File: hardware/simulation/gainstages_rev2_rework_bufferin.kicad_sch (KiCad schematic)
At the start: 25 parts, among them U1 ${SIM.PARAMS}, U2 ${SIM.PARAMS}, U3 ${SIM.PARAMS}

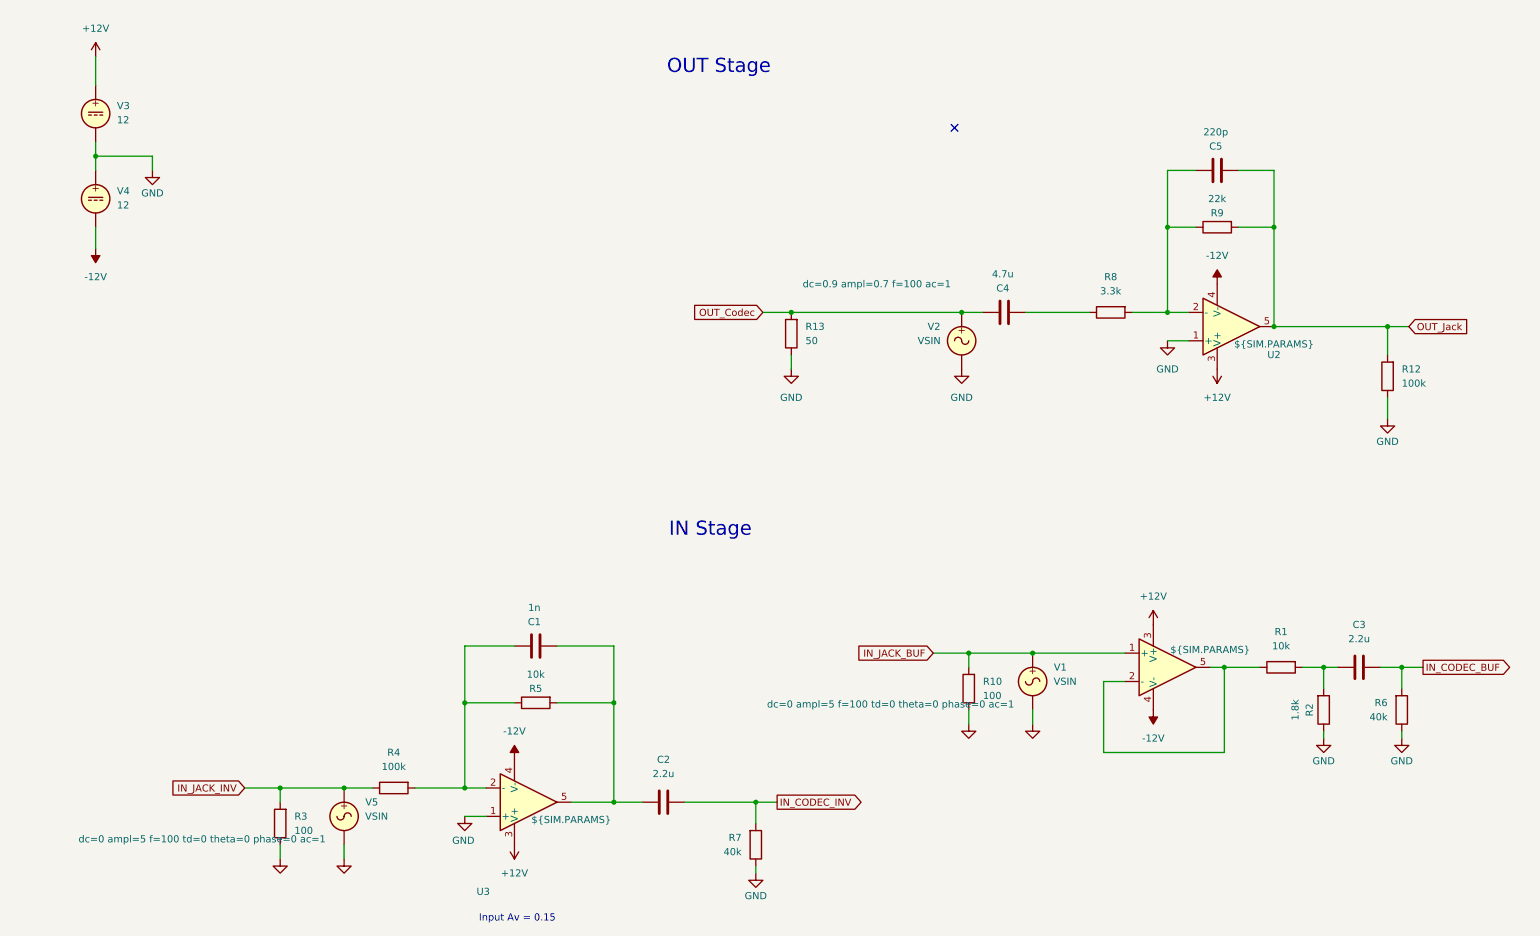
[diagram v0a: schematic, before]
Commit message: hwardware: update analog stages simulation
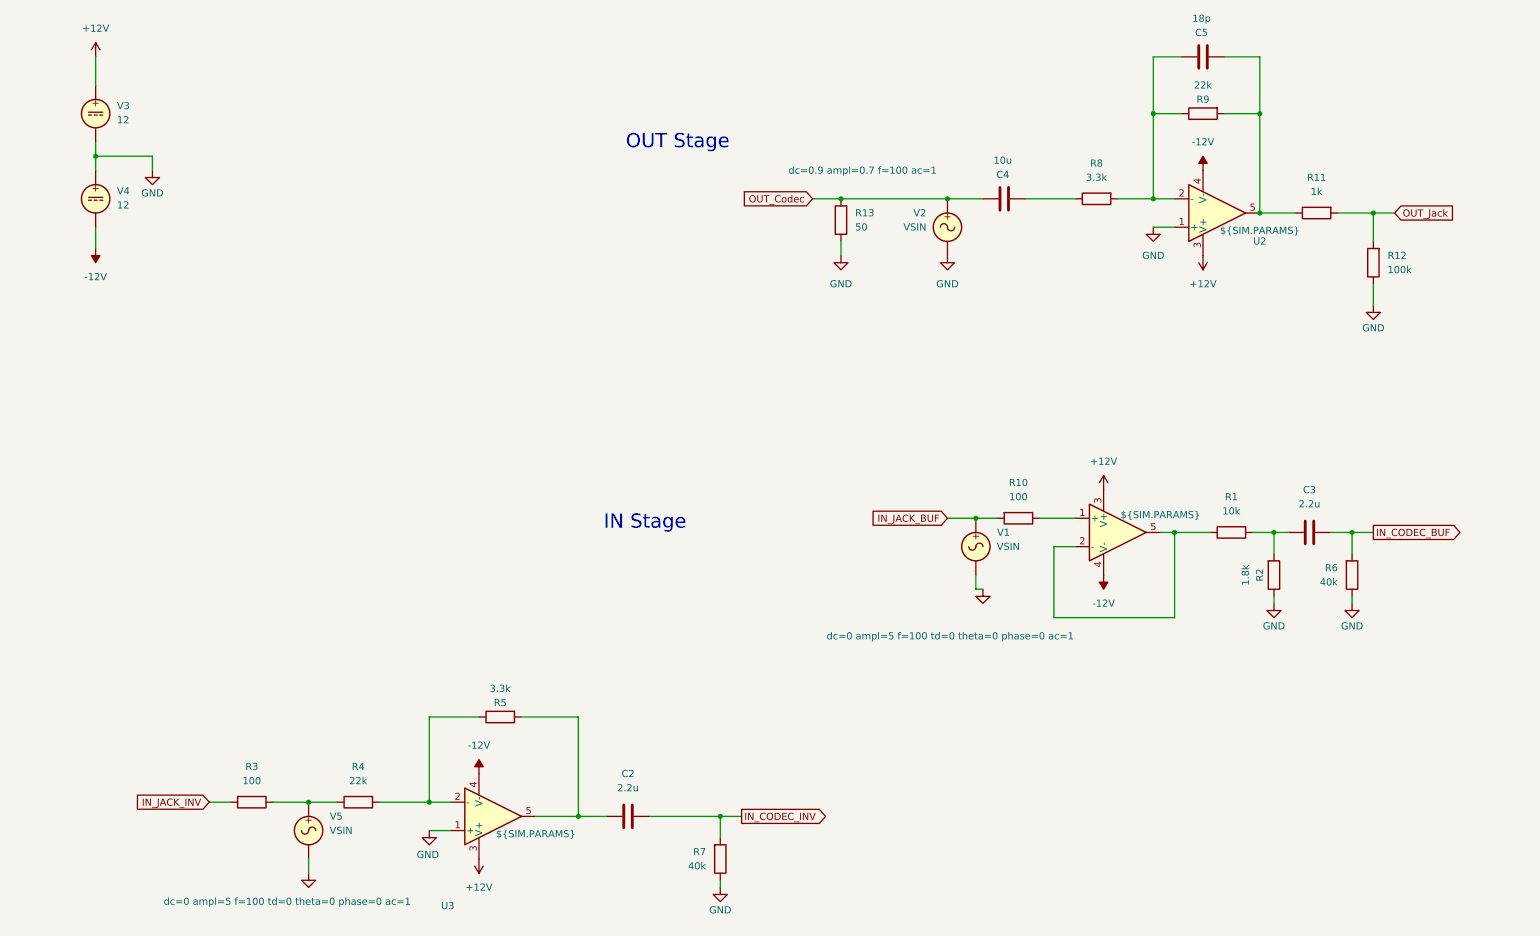
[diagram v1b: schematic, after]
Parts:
- removed C1: 1n, symbol Device:C
- added R11: 1k, symbol Device:R
- C4: value 4.7u -> 10u
- C5: value 220p -> 18p
- R4: value 100k -> 22k
- R5: value 10k -> 3.3k
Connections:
- net GND: no longer R10.1, R3.1
- net IN_JACK_BUF: no longer U1.1 (+)
- net IN_JACK_INV: no longer R4.1, V5.1
- net OUT_Jack: now also R11.2; no longer C5.1, R9.2, U2.5
- new net: R3.1, R4.1, V5.1
- new net: R10.1, U1.1 (+)
- new net: C5.1, R11.1, R9.2, U2.5
- no-connect marks 1 -> 0
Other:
- note removed: "Input Av = 0.15"
- moved on the sheet: C2, C3, C4, C5, R1, R12, R13, R2, R3, R4, R5, R6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

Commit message: hardware: update analog sim and routing (wip)
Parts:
- removed C5: 18p, symbol Device:C
- added C1: 18p, symbol Device:C
- added D1, D2: D_Schottky, symbol Device:D_Schottky
- added V10: 1.8, symbol Simulation_SPICE:VDC
- added V6: 3.3, symbol Simulation_SPICE:VDC
- added V7: 0.9, symbol Simulation_SPICE:VDC
- added V8, V9: VPULSE, symbol Simulation_SPICE:VPULSE
- R1: value 10k -> 12k
- R8: value 3.3k -> 5.6k
- R9: value 22k -> 39k
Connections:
- net GND: now also D2.1 (K), V10.2, V6.2, V7.2, V8.2, V9.2; no longer R13.1, R6.1
- net IN_CODEC_BUF: now also D1.1 (K), D2.2 (A)
- net IN_JACK_BUF: now also V9.1
- net OUT_Codec: now also V8.1; no longer C4.2
- net at R8.2, R9.1, U2.2 (-): now also C1.2
- net at R11.1, R9.2, U2.5: now also C1.1
- new net: R6.1, V7.1
- new net: C4.2, R13.1
- new net +1V8: D1.2 (A), V10.1
- new net +3V3: V6.1
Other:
- note added: "ADC absolute input limits: Input pins must remain within -0.3 V to (A_VDD + 0.3 V). Since A_VDD = 1.8 V (generated by the TLV320AIC internal LDO), the maximum allowed input voltage is 2.1 V. Therefore a voltage divider of 1.8k/12k=0.15 is used to attenuate the signal. The attenuation yields a peak voltage of 2.11V at -+10V input signal, which is just within the limits of the ADC. Such high signal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"
- note added: "CM (Common Mode) voltage of 0.9V"
- note added: "DAC Output Impedance"
- note added: "Downstream Input Impedance"
- note added: "Input AC Coupling filter Cutoff frequency f_c = 1/2*pi*R1*C3 = 1.809Hz"
- note added: "Input AC Coupling filter Cutoff frequency f_c = 1/2*pi*R13*C4 = 2.842Hz"
- note added: "Stabilization Filter prohibits Opamp Oscillation by input stray capacitances (not simulated) Cutoff frequency f = 1/2*pi*39E3*18E-12 = 226.716kHz"
- moved on the sheet: C2, C3, C4, R1, R10, R11, R12, R13, R2, R3, R4, R5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

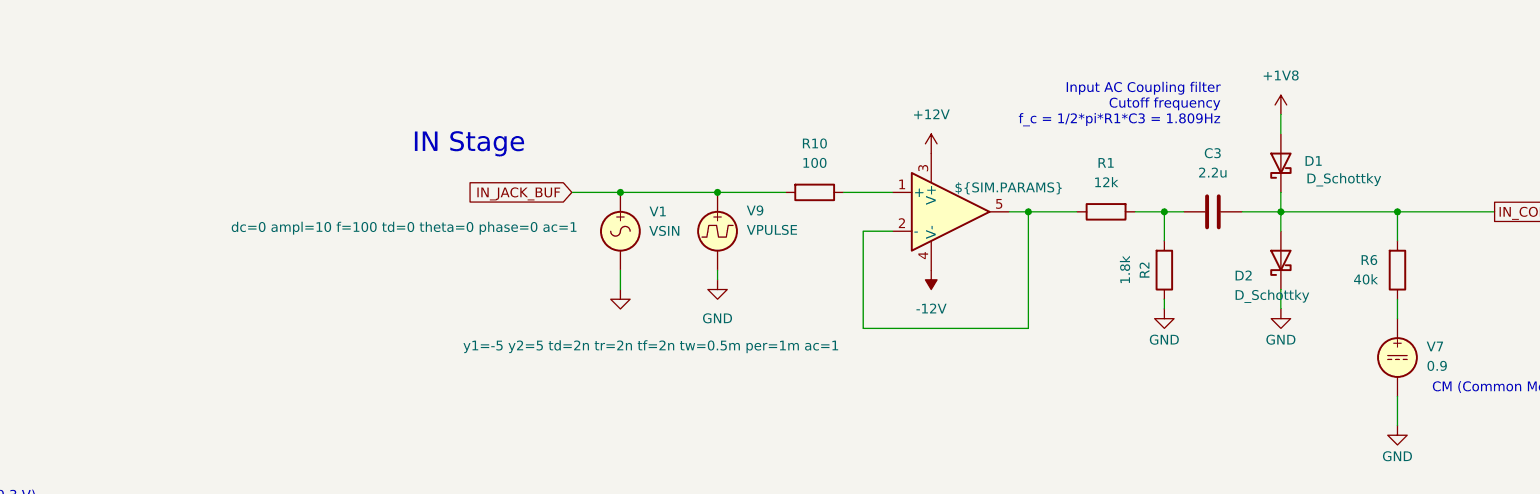
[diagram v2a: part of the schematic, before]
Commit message: sim: update simulation schematic and libraries
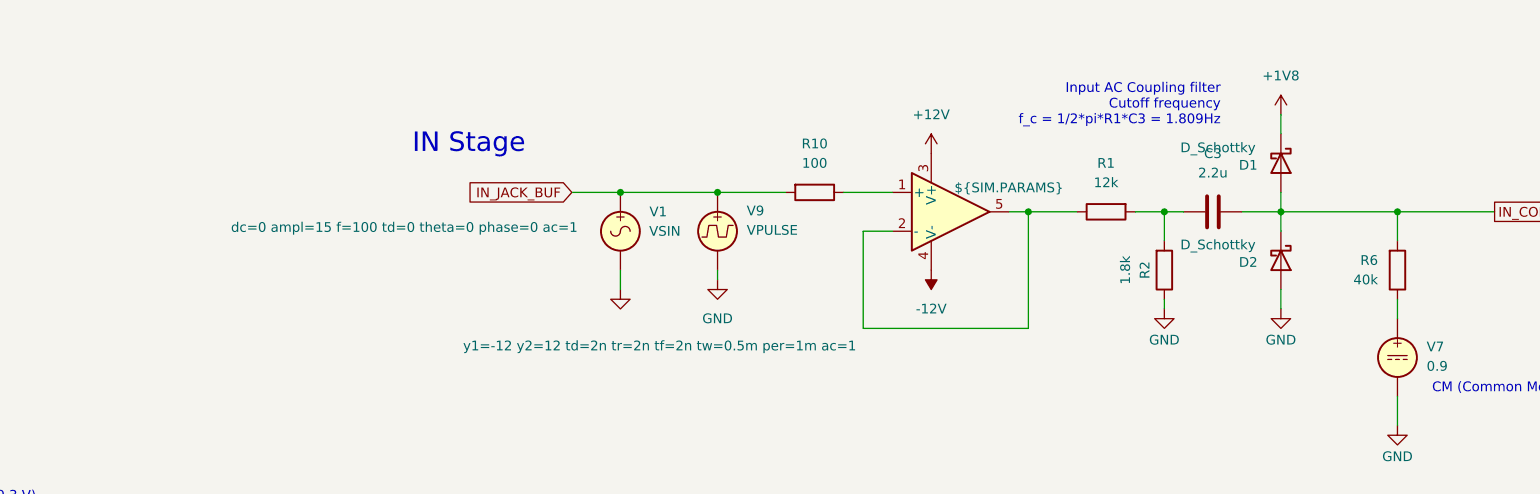
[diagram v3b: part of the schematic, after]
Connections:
- net +1V8: now also D1.1 (K); no longer D1.2 (A)
- net GND: now also D2.2 (A); no longer D2.1 (K)
- net IN_CODEC_BUF: now also D1.2 (A), D2.1 (K); no longer D1.1 (K), D2.2 (A)
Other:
- moved on the sheet: D1
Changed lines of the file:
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@@
 			)
 		)
-		(property "Sim.Pins" "1=1 2=2 3=3 4=4 5=5"
+		(property "Sim.Pins" "1=in+ 2=in- 3=vcc 4=vee 5=out"
 			(at 203.2 69.85 0)
 			(effects
@@
 			)
 		)
-		(property "Sim.Library" "/home/jonas/Downloads/NE5532.lib"
+		(property "Sim.Library" "${KICAD7_SYMBOL_DIR}/Simulation_SPICE.sp"
 			(at 203.2 69.85 0)
 			(effects
@@
 			)
 		)
-		(property "Sim.Name" "NE5532"
+		(property "Sim.Name" "kicad_builtin_opamp"
 			(at 203.2 69.85 0)
 			(effects
@@
 	)
 	(symbol
-		(lib_id "Device:D_Schottky")
-		(at 231.14 135.89 90)
-		(unit 1)
-		(exclude_from_sim no)
-		(in_bom yes)
-		(on_board yes)
-		(dnp no)
-		(property "Reference" "D2"
-			(at 225.044 137.922 90)
-			(effects
-				(font
-					(size 1.27 1.27)
-				)
-				(justify right)
-			)
-		)
-		(property "Value" "D_Schottky"
-			(at 225.044 140.462 90)
-			(effects
-				(font
-					(size 1.27 1.27)
-				)
-				(justify right)
-			)
-		)
-		(property "Footprint" ""
-			(at 231.14 135.89 0)
-			(effects
-				(font
-					(size 1.27 1.27)
-				)
-				(hide yes)
-			)
-		)
-		(property "Datasheet" "~"
-			(at 231.14 135.89 0)
-			(effects
-				(font
-					(size 1.27 1.27)
-				)
-				(hide yes)
-			)
-		)
-		(property "Description" "Schottky diode"
-			(at 231.14 135.89 0)
-			(effects
-				(font
-					(size 1.27 1.27)
-				)
-				(hide yes)
-			)
-		)
-		(property "Sim.Library" "/home/jonas/Downloads/BAT54.spice.txt"
-			(at 231.14 135.89 0)
-			(effects
-				(font
-					(size 1.27 1.27)
-				)
-				(hide yes)
-			)
-		)
-		(property "Sim.Name" "BAT54"
-			(at 231.14 135.89 0)
-			(effects
-				(font
-					(size 1.27 1.27)
-				)
-				(hide yes)
-			)
-		)
-		(property "Sim.Device" "D"
-			(at 231.14 135.89 0)
-			(effects
-				(font
-					(size 1.27 1.27)
-				)
-				(hide yes)
-			)
-		)
-		(property "Sim.Pins" "1=A 2=K"
-			(at 231.14 135.89 0)
-			(effects
-				(font
-					(size 1.27 1.27)
-				)
-				(hide yes)
-			)
-		)
-		(pin "1"
-		)
-		(pin "2"
-		)
-		(instances
-			(project "gainstages_rev2_rework_bufferin"
-				(path "/934635e5-59a1-4479-8af1-a5a6d88fcf47"
-					(reference "D2")
-					(unit 1)
-				)
-			)
-		)
-	)
-	(symbol
 		(lib_id "power:GND")
 		(at 133.35 80.01 0)
@@
 		(mirror y)
 		(unit 1)
-		(exclude_from_sim yes)
+		(exclude_from_sim no)
 		(in_bom no)
 		(on_board no)
@@
 			)
 		)
-		(property "Sim.Params" "dc=0 ampl=10 f=100 td=0 theta=0 phase=0 ac=1"
+		(property "Sim.Params" "dc=0 ampl=15 f=100 td=0 theta=0 phase=0 ac=1"
 			(at 139.192 131.572 0)
 			(effects
@@
 		(at 157.48 132.08 0)
 		(unit 1)
-		(exclude_from_sim no)
+		(exclude_from_sim yes)
 		(in_bom yes)
 		(on_board yes)
@@
 			)
 		)
-		(property "Sim.Params" "y1=-5 y2=5 td=2n tr=2n tf=2n tw=0.5m per=1m ac=1"
+		(property "Sim.Params" "y1=-12 y2=12 td=2n tr=2n tf=2n tw=0.5m per=1m ac=1"
 			(at 124.206 147.066 0)
 			(effects
@@
 	(symbol
 		(lib_id "Device:D_Schottky")
-		(at 231.14 123.19 90)
+		(at 231.14 123.19 270)
 		(unit 1)
 		(exclude_from_sim no)
@@
 		(dnp no)
 		(property "Reference" "D1"
-			(at 234.188 122.936 90)
+			(at 228.092 123.444 90)
 			(effects
 				(font
@@
 		)
 		(property "Value" "D_Schottky"
-			(at 234.442 125.222 90)
+			(at 227.838 121.158 90)
 			(effects
 				(font
@@
 			)
 		)
-		(property "Sim.Library" "/home/jonas/Downloads/BAT54.spice.txt"
+		(property "Sim.Library" "spice_models/BAT54.spice.txt"
 			(at 231.14 123.19 0)
 			(effects
@@
 			)
 		)
-		(property "Sim.Pins" "1=A 2=K"
+		(property "Sim.Pins" "1=K 2=A"
 			(at 231.14 123.19 0)
 			(effects
@@
 					(unit 1)
 				)
+			)
+		)
+	)
+	(symbol
+		(lib_id "Device:D_Schottky")
+		(at 231.14 135.89 270)
+		(unit 1)
+		(exclude_from_sim no)
+		(in_bom yes)
+		(on_board yes)
+		(dnp no)
+		(property "Reference" "D2"
+			(at 228.092 136.144 90)
+			(effects
+				(font
+					(size 1.27 1.27)
+				)
+				(justify right)
+			)
+		)
+		(property "Value" "D_Schottky"
+			(at 227.838 133.858 90)
+			(effects
+				(font
+					(size 1.27 1.27)
+				)
+				(justify right)
+			)
+		)
+		(property "Footprint" ""
+			(at 231.14 135.89 0)
+			(effects
+				(font
+					(size 1.27 1.27)
+				)
+				(hide yes)
+			)
+		)
+		(property "Datasheet" "~"
+			(at 231.14 135.89 0)
+			(effects
+				(font
+					(size 1.27 1.27)
+				)
+				(hide yes)
+			)
+		)
+		(property "Description" "Schottky diode"
+			(at 231.14 135.89 0)
+			(effects
+				(font
+					(size 1.27 1.27)
+				)
+				(hide yes)
+			)
+		)
+		(property "Sim.Library" "spice_models/BAT54.spice.txt"
+			(at 231.14 135.89 0)
+			(effects
+				(font
+					(size 1.27 1.27)
+				)
+				(hide yes)
+			)
+		)
+		(property "Sim.Name" "BAT54"
+			(at 231.14 135.89 0)
+			(effects
+				(font
+					(size 1.27 1.27)
+				)
+				(hide yes)
+			)
+		)
+		(property "Sim.Device" "D"
+			(at 231.14 135.89 0)
+			(effects
+				(font
+					(size 1.27 1.27)
+				)
+				(hide yes)
+			)
+		)
+		(property "Sim.Pins" "1=K 2=A"
+			(at 231.14 135.89 0)
+			(effects
+				(font
+					(size 1.27 1.27)
+				)
+				(hide yes)
+			)
+		)
+		(pin "1"
+		)
+		(pin "2"
+		)
+		(instances
+			(project "gainstages_rev2_rework_bufferin"
+				(path "/934635e5-59a1-4479-8af1-a5a6d88fcf47"
+					(reference "D2")
+					(unit 1)
+				)

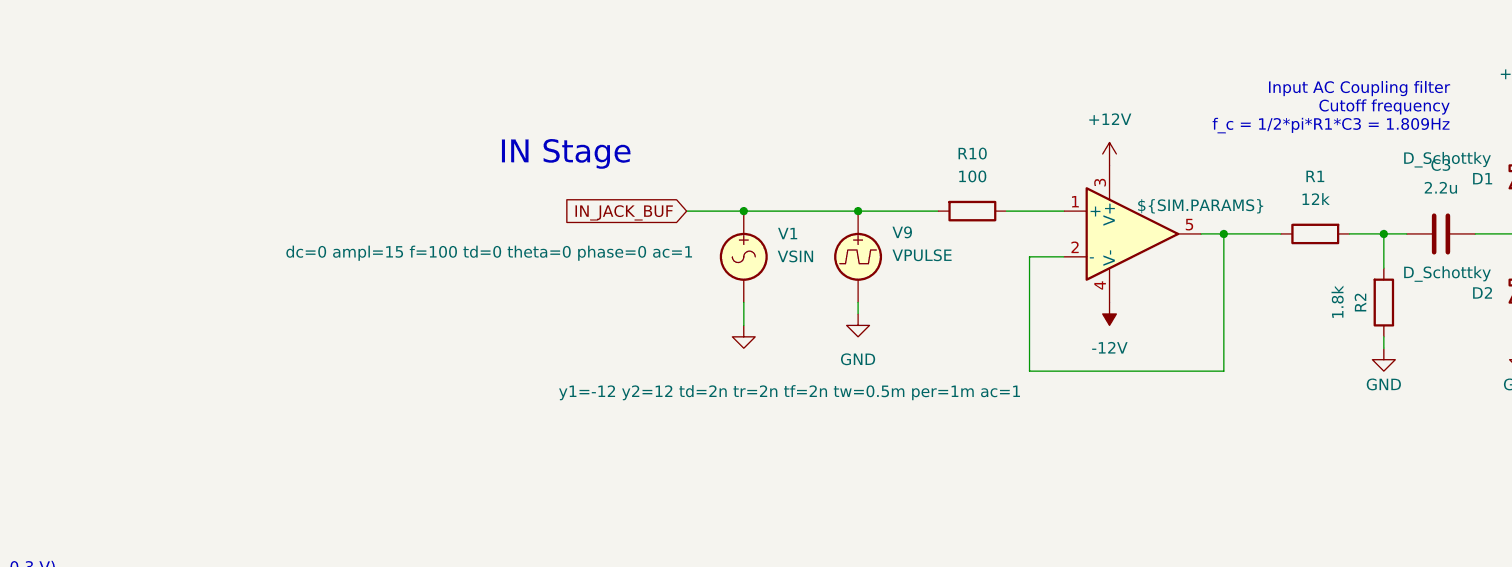
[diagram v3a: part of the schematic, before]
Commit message: feat: fixes in pcb design
- use correct BAT54S placement/layout
- fix pin mapping of fade potentiometers, also adjust routing
- switch pins that did not support PWM out (for fader led)
- switch pins that did not support EXTI
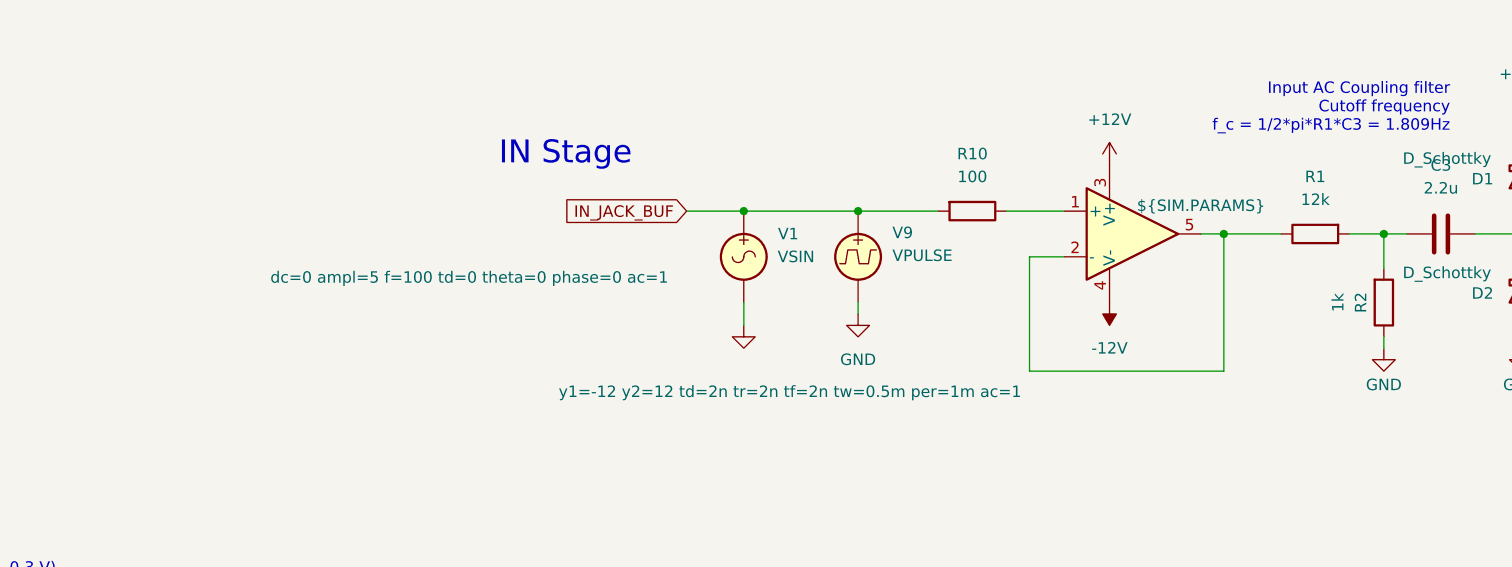
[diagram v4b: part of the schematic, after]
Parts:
- R2: value 1.8k -> 1k
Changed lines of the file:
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@@
 			)
 		)
-		(property "Sim.Params" "dc=0 ampl=15 f=100 td=0 theta=0 phase=0 ac=1"
-			(at 139.192 131.572 0)
+		(property "Sim.Params" "dc=0 ampl=5 f=100 td=0 theta=0 phase=0 ac=1"
+			(at 136.398 134.366 0)
 			(effects
 				(font
@@
 			)
 		)
-		(property "Value" "1.8k"
+		(property "Value" "1k"
 			(at 210.82 137.16 90)
 			(effects
